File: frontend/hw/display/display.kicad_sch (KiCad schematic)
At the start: 16 parts, among them J1 Conn_01x04, J2 Conn_02x17_Odd_Even, Q1 MMBT3904, Q2 MMBT3904, SW1 SW_Push, U1 ESP32-WROOM-32U, U2 CH340C, U3 AMS1117-3.3

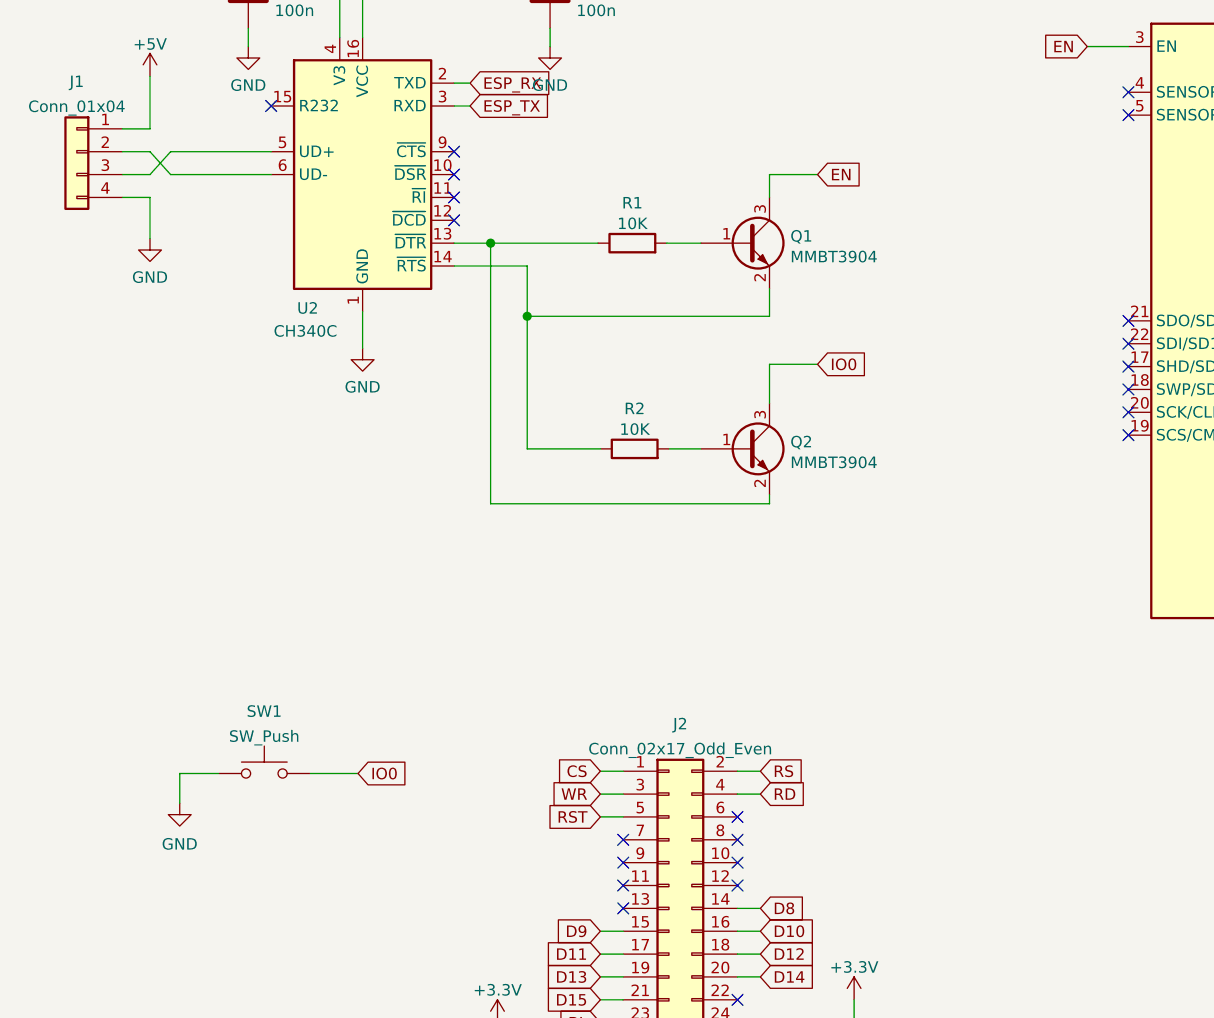
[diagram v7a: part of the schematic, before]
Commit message: Add buttons.
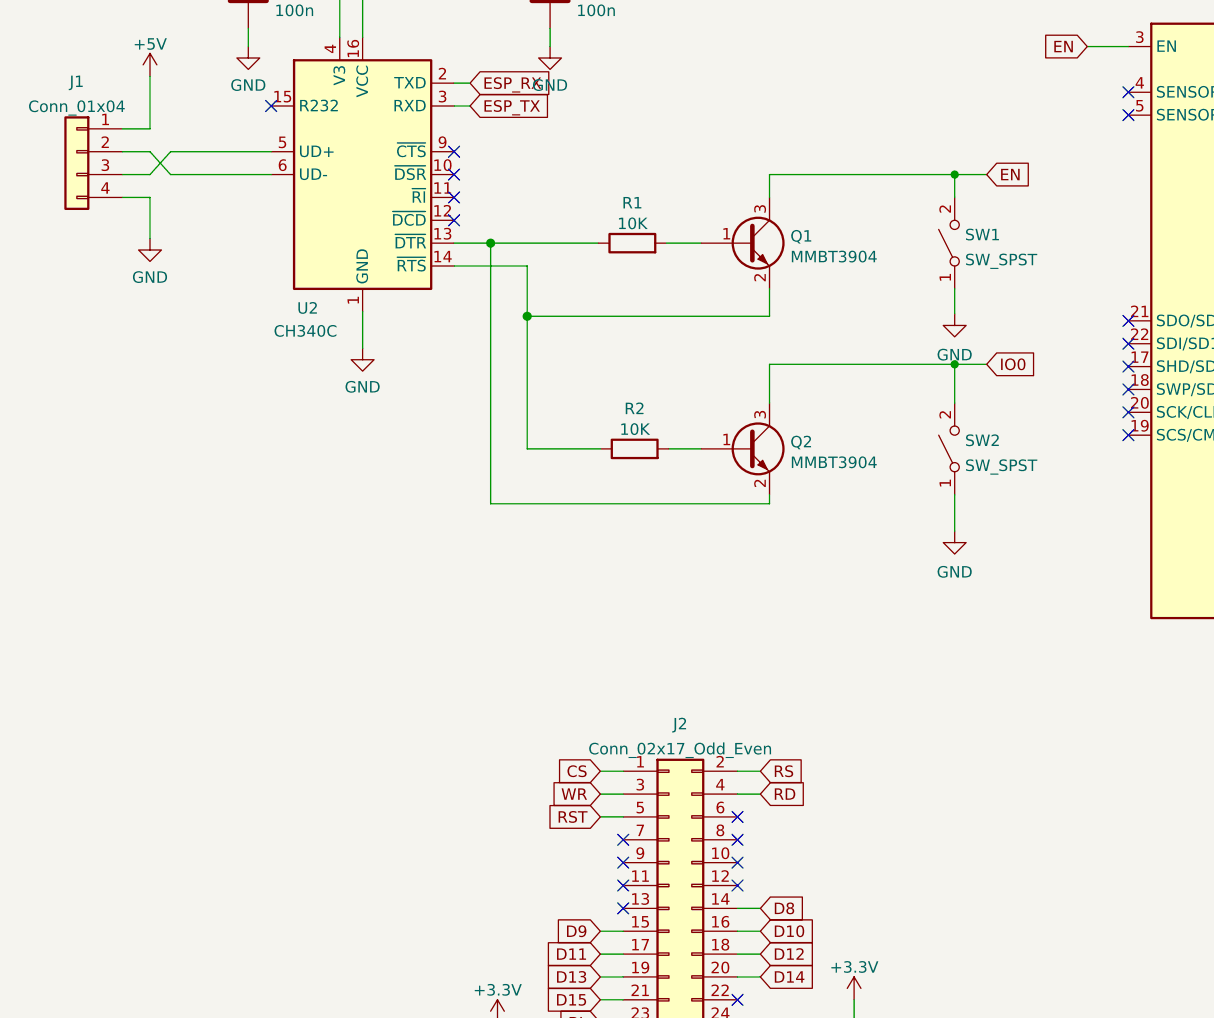
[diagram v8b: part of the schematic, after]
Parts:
- removed SW1: SW_Push, Button_Switch_SMD:SW_Push_SPST_NO_Alps_SKRK, symbol Switch:SW_Push
- added SW1, SW2: SW_SPST, Button_Switch_SMD:SW_SPST_CK_RS282G05A3, symbol Switch:SW_SPST
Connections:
- net EN: now also SW1.2 (B)
- net GND: now also SW1.1 (A), SW2.1 (A)
- net IO0: now also SW2.2 (B)
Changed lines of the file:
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@@
   (junction (at 55.88 39.116) (diameter 1.016) (color 0 0 0 0)
   )
+  (junction (at 121.666 87.122) (diameter 0) (color 0 0 0 0)
+  )
   (junction (at 70.104 73.66) (diameter 1.016) (color 0 0 0 0)
   )
@@
   )
   (junction (at 225.552 49.784) (diameter 1.016) (color 0 0 0 0)
+  )
+  (junction (at 121.666 66.04) (diameter 0) (color 0 0 0 0)
   )
   (junction (at 209.296 38.862) (diameter 1.016) (color 0 0 0 0)
@@
     (stroke (width 0) (type solid) (color 0 0 0 0))
   )
-  (wire (pts (xy 35.56 135.89) (xy 35.56 132.588))
-    (stroke (width 0) (type default) (color 0 0 0 0))
-  )
   (wire (pts (xy 82.296 170.434) (xy 84.836 170.434))
     (stroke (width 0) (type default) (color 0 0 0 0))
@@
     (stroke (width 0) (type default) (color 0 0 0 0))
   )
+  (wire (pts (xy 121.666 66.04) (xy 121.666 68.58))
+    (stroke (width 0) (type default) (color 0 0 0 0))
+  )
   (wire (pts (xy 76.708 49.784) (xy 76.708 51.816))
     (stroke (width 0) (type solid) (color 0 0 0 0))
@@
     (stroke (width 0) (type solid) (color 0 0 0 0))
   )
+  (wire (pts (xy 121.666 78.74) (xy 121.666 81.534))
+    (stroke (width 0) (type default) (color 0 0 0 0))
+  )
   (wire (pts (xy 171.45 92.456) (xy 178.054 92.456))
     (stroke (width 0) (type default) (color 0 0 0 0))
@@
     (stroke (width 0) (type solid) (color 0 0 0 0))
   )
+  (wire (pts (xy 121.666 101.6) (xy 121.666 105.664))
+    (stroke (width 0) (type default) (color 0 0 0 0))
+  )
   (wire (pts (xy 32.258 55.118) (xy 32.258 60.96))
     (stroke (width 0) (type default) (color 0 0 0 0))
@@
     (stroke (width 0) (type solid) (color 0 0 0 0))
   )
-  (wire (pts (xy 106.426 66.04) (xy 101.092 66.04))
+  (wire (pts (xy 101.092 66.04) (xy 121.666 66.04))
     (stroke (width 0) (type solid) (color 0 0 0 0))
   )
@@
     (stroke (width 0) (type default) (color 0 0 0 0))
   )
+  (wire (pts (xy 121.666 66.04) (xy 125.222 66.04))
+    (stroke (width 0) (type solid) (color 0 0 0 0))
+  )
   (wire (pts (xy 97.536 152.654) (xy 100.076 152.654))
     (stroke (width 0) (type default) (color 0 0 0 0))
@@
     (stroke (width 0) (type default) (color 0 0 0 0))
   )
-  (wire (pts (xy 50.038 132.588) (xy 55.372 132.588))
-    (stroke (width 0) (type default) (color 0 0 0 0))
+  (wire (pts (xy 121.666 87.122) (xy 125.222 87.122))
+    (stroke (width 0) (type solid) (color 0 0 0 0))
   )
   (wire (pts (xy 171.45 61.976) (xy 177.546 61.976))
@@
     (stroke (width 0) (type solid) (color 0 0 0 0))
   )
+  (wire (pts (xy 121.666 87.122) (xy 121.666 91.44))
+    (stroke (width 0) (type default) (color 0 0 0 0))
+  )
   (wire (pts (xy 97.536 167.894) (xy 100.076 167.894))
     (stroke (width 0) (type default) (color 0 0 0 0))
@@
     (stroke (width 0) (type default) (color 0 0 0 0))
   )
-  (wire (pts (xy 35.56 132.588) (xy 39.878 132.588))
-    (stroke (width 0) (type default) (color 0 0 0 0))
-  )
   (wire (pts (xy 156.21 31.75) (xy 156.21 35.052))
     (stroke (width 0) (type solid) (color 0 0 0 0))
@@
     (stroke (width 0) (type solid) (color 0 0 0 0))
   )
-  (wire (pts (xy 106.426 87.122) (xy 101.092 87.122))
+  (wire (pts (xy 101.092 87.122) (xy 121.666 87.122))
     (stroke (width 0) (type solid) (color 0 0 0 0))
   )
@@
     )
   )
-  (global_label "IO0" (shape input) (at 55.372 132.588 0) (fields_autoplaced)
-    (effects (font (size 1.27 1.27)) (justify left))
-    (property "Intersheet References" "${INTERSHEET_REFS}" (id 0) (at 61.1204 132.5086 0)
-      (effects (font (size 1.27 1.27)) (justify left) hide)
-    )
-  )
   (global_label "CS" (shape input) (at 82.296 132.334 180) (fields_autoplaced)
     (effects (font (size 1.27 1.27)) (justify right))
@@
     )
   )
-  (global_label "EN" (shape input) (at 106.426 66.04 0) (fields_autoplaced)
-    (effects (font (size 1.27 1.27)) (justify left))
-    (property "Intersheet References" "${INTERSHEET_REFS}" (id 0) (at 111.3186 65.9606 0)
-      (effects (font (size 1.27 1.27)) (justify left) hide)
-    )
-  )
-  (global_label "IO0" (shape input) (at 106.426 87.122 0) (fields_autoplaced)
-    (effects (font (size 1.27 1.27)) (justify left))
-    (property "Intersheet References" "${INTERSHEET_REFS}" (id 0) (at 111.9839 87.0426 0)
+  (global_label "EN" (shape input) (at 125.222 66.04 0) (fields_autoplaced)
+    (effects (font (size 1.27 1.27)) (justify left))
+    (property "Intersheet References" "${INTERSHEET_REFS}" (id 0) (at 130.1146 65.9606 0)
+      (effects (font (size 1.27 1.27)) (justify left) hide)
+    )
+  )
+  (global_label "IO0" (shape input) (at 125.222 87.122 0) (fields_autoplaced)
+    (effects (font (size 1.27 1.27)) (justify left))
+    (property "Intersheet References" "${INTERSHEET_REFS}" (id 0) (at 130.7799 87.0426 0)
       (effects (font (size 1.27 1.27)) (justify left) hide)
     )
@@
     (pin "1")
   )
-  (symbol (lib_id "Switch:SW_Push") (at 44.958 132.588 0) (unit 1)
-    (in_bom yes) (on_board yes) (fields_autoplaced)
-    (property "Reference" "SW1" (id 0) (at 44.958 125.7005 0))
-    (property "Value" "SW_Push" (id 1) (at 44.958 128.4756 0))
-    (property "Footprint" "Button_Switch_SMD:SW_Push_SPST_NO_Alps_SKRK" (id 2) (at 44.958 127.508 0)
-      (effects (font (size 1.27 1.27)) hide)
-    )
-    (property "Datasheet" "~" (id 3) (at 44.958 127.508 0)
+  (symbol (lib_id "Switch:SW_SPST") (at 121.666 96.52 90) (unit 1)
+    (in_bom yes) (on_board yes) (fields_autoplaced)
+    (property "Reference" "SW2" (id 0) (at 122.809 95.6115 90)
+      (effects (font (size 1.27 1.27)) (justify right))
+    )
+    (property "Value" "SW_SPST" (id 1) (at 122.809 98.3866 90)
+      (effects (font (size 1.27 1.27)) (justify right))
+    )
+    (property "Footprint" "Button_Switch_SMD:SW_SPST_CK_RS282G05A3" (id 2) (at 121.666 96.52 0)
+      (effects (font (size 1.27 1.27)) hide)
+    )
+    (property "Datasheet" "~" (id 3) (at 121.666 96.52 0)
       (effects (font (size 1.27 1.27)) hide)
     )
@@
     )
     (property "Datasheet" "" (id 3) (at 217.678 81.534 0)
+      (effects (font (size 1.27 1.27)) hide)
+    )
+    (pin "1")
+  )
+  (symbol (lib_id "power:GND") (at 121.666 81.534 0) (unit 1)
+    (in_bom yes) (on_board yes) (fields_autoplaced)
+    (property "Reference" "#PWR02" (id 0) (at 121.666 87.884 0)
+      (effects (font (size 1.27 1.27)) hide)
+    )
+    (property "Value" "GND" (id 1) (at 121.666 86.0965 0))
+    (property "Footprint" "" (id 2) (at 121.666 81.534 0)
+      (effects (font (size 1.27 1.27)) hide)
+    )
+    (property "Datasheet" "" (id 3) (at 121.666 81.534 0)
       (effects (font (size 1.27 1.27)) hide)
     )
@@
     (pin "9")
   )
+  (symbol (lib_id "Switch:SW_SPST") (at 121.666 73.66 90) (unit 1)
+    (in_bom yes) (on_board yes) (fields_autoplaced)
+    (property "Reference" "SW1" (id 0) (at 122.809 72.7515 90)
+      (effects (font (size 1.27 1.27)) (justify right))
+    )
+    (property "Value" "SW_SPST" (id 1) (at 122.809 75.5266 90)
+      (effects (font (size 1.27 1.27)) (justify right))
+    )
+    (property "Footprint" "Button_Switch_SMD:SW_SPST_CK_RS282G05A3" (id 2) (at 121.666 73.66 0)
+      (effects (font (size 1.27 1.27)) hide)
+    )
+    (property "Datasheet" "~" (id 3) (at 121.666 73.66 0)
+      (effects (font (size 1.27 1.27)) hide)
+    )
+    (pin "1")
+    (pin "2")
+  )
   (symbol (lib_id "Device:CP") (at 217.678 88.646 0) (unit 1)
     (in_bom yes) (on_board yes) (fields_autoplaced)
@@
     (pin "1")
   )
-  (symbol (lib_id "power:GND") (at 35.56 135.89 0) (unit 1)
-    (in_bom yes) (on_board yes) (fields_autoplaced)
-    (property "Reference" "#PWR01" (id 0) (at 35.56 142.24 0)
-      (effects (font (size 1.27 1.27)) hide)
-    )
-    (property "Value" "GND" (id 1) (at 35.56 140.4525 0))
-    (property "Footprint" "" (id 2) (at 35.56 135.89 0)
-      (effects (font (size 1.27 1.27)) hide)
-    )
-    (property "Datasheet" "" (id 3) (at 35.56 135.89 0)
-      (effects (font (size 1.27 1.27)) hide)
-    )
-    (pin "1")
-  )
   (symbol (lib_id "power:GND") (at 174.498 44.45 0) (unit 1)
     (in_bom yes) (on_board yes) (fields_autoplaced)
@@
     (pin "1")
   )
+  (symbol (lib_id "power:GND") (at 121.666 105.664 0) (unit 1)
+    (in_bom yes) (on_board yes) (fields_autoplaced)
+    (property "Reference" "#PWR03" (id 0) (at 121.666 112.014 0)
+      (effects (font (size 1.27 1.27)) hide)
+    )
+    (property "Value" "GND" (id 1) (at 121.666 110.2265 0))
+    (property "Footprint" "" (id 2) (at 121.666 105.664 0)
+      (effects (font (size 1.27 1.27)) hide)
+    )
+    (property "Datasheet" "" (id 3) (at 121.666 105.664 0)
+      (effects (font (size 1.27 1.27)) hide)
+    )
+    (pin "1")
+  )
   (symbol (lib_id "power:+5V") (at 32.258 55.118 0) (unit 1)
     (in_bom yes) (on_board yes) (fields_autoplaced)
@@
       (reference "#FLG0101") (unit 1) (value "PWR_FLAG") (footprint "")
     )
-    (path "/af5b0949-f220-41df-9675-e4adeb75ceb0"
-      (reference "#PWR01") (unit 1) (value "GND") (footprint "")
+    (path "/5ba7fda8-0d64-46a0-9c08-86824094384f"
+      (reference "#PWR02") (unit 1) (value "GND") (footprint "")
+    )
+    (path "/cddcd9e2-2e24-456e-be07-f55236555161"
+      (reference "#PWR03") (unit 1) (value "GND") (footprint "")
     )
     (path "/f3787df9-6344-42f0-b474-f781ef32cc09"
@@
       (reference "R2") (unit 1) (value "10K") (footprint "Resistor_SMD:R_0603_1608Metric")
     )
-    (path "/11316c6e-c6b6-4377-9342-a7648e7f77be"
-      (reference "SW1") (unit 1) (value "SW_Push") (footprint "Button_Switch_SMD:SW_Push_SPST_NO_Alps_SKRK")
+    (path "/8f29ec2b-5253-4ae2-bf8f-40e83998f739"
+      (reference "SW1") (unit 1) (value "SW_SPST") (footprint "Button_Switch_SMD:SW_SPST_CK_RS282G05A3")
+    )
+    (path "/14402da7-aa14-4f51-9c77-4cb07e5abca1"
+      (reference "SW2") (unit 1) (value "SW_SPST") (footprint "Button_Switch_SMD:SW_SPST_CK_RS282G05A3")
     )
     (path "/647440a9-0aaf-4b33-9087-36e43e3aa36f"
